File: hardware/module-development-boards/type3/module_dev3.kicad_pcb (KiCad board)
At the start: 2 copper layers, 30 x 26 mm, 28 parts, among them J1 SensorHub_Module_CONN_V1, J12 Conn_01x01, J13 Conn_01x01, J14 Conn_01x01, J15 Conn_01x01, J16 Conn_01x01, J17 Conn_01x01, J18 Conn_01x01, J19 Conn_01x01, J21 Conn_01x01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

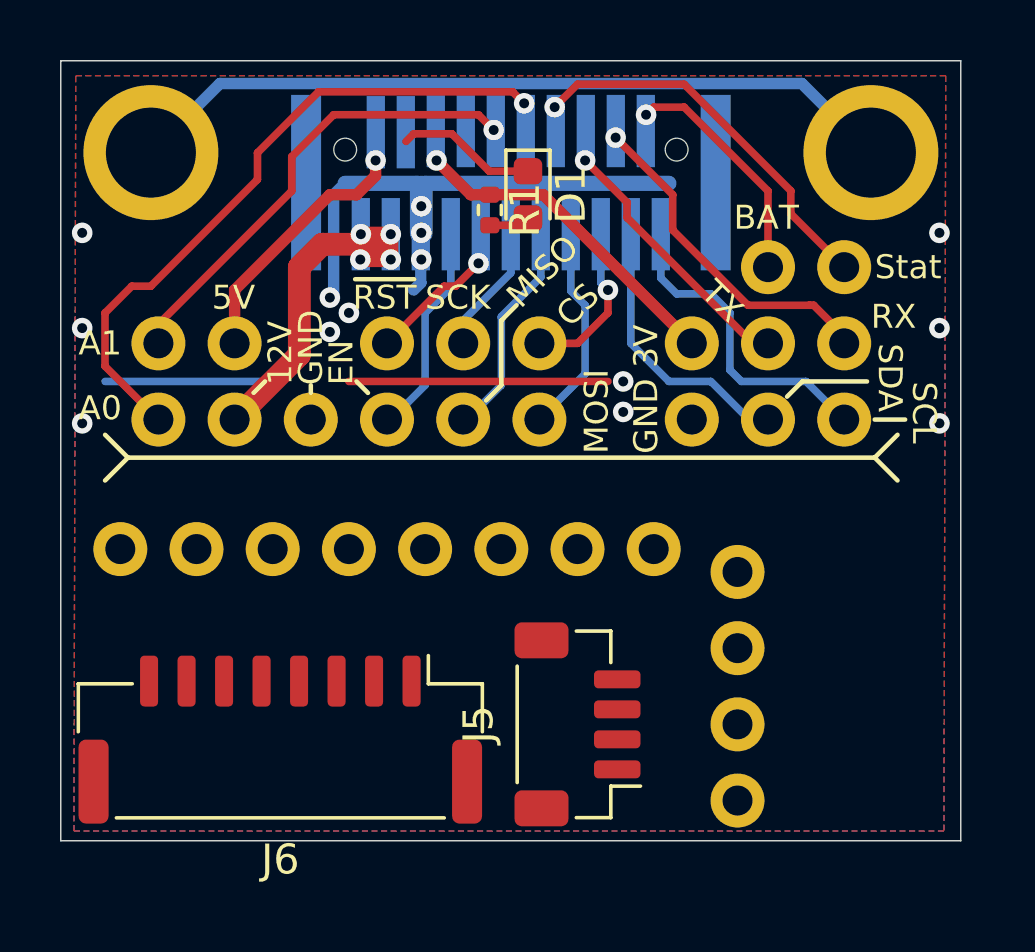
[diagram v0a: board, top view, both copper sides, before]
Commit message: cleanup dev board type 3
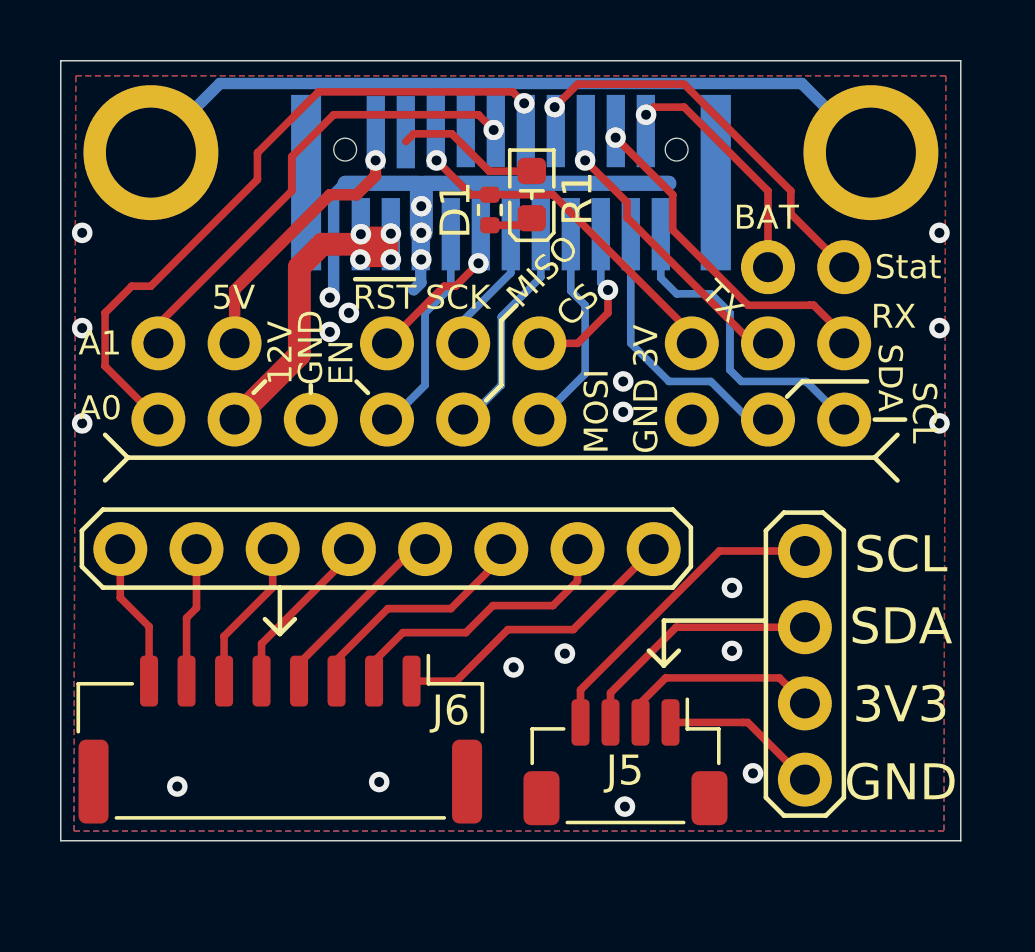
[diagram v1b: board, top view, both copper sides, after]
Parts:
- D1: value D_LED_0603_Red -> LED_0603_Red; footprint LED_SMD:LED_0603_1608Metric -> jlcsmt:LED_0603_1608Metric
- J1: value SensorHub_Module_CONN_V1 -> LegoSENSE_Module_CONN_V1
- moved J3 8.62 mm to (116.8, 77.3), turned to 0 degrees
- moved J5 2.04 mm to (110.8, 84.3), turned to 180 degrees
- moved D1 0.13 mm to (107.7, 65.4), turned to 90 degrees
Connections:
- net /~RST renamed /~{RST}
- D1 pad 2: Net-(D1-Pad2) -> (no net)
- R1 pad 2: Net-(D1-Pad2) -> (no net)
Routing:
- net GND: track 65.5 -> 49.0 mm, vias 14 -> 22
- net Net-(J3-Pad1): track 0.00 -> 10.5 mm
- net Net-(J4-Pad8): track 0.00 -> 9.89 mm
- net Net-(J4-Pad7): track 0.00 -> 9.61 mm
- net Net-(J3-Pad2): track 0.00 -> 8.37 mm
- net Net-(J4-Pad6): track 0.00 -> 7.90 mm
- net Net-(J3-Pad3): track 0.00 -> 6.83 mm
- net Net-(J4-Pad5): track 0.00 -> 6.37 mm
- net Net-(J4-Pad4): track 0.00 -> 5.61 mm
- net Net-(J3-Pad4): track 0.00 -> 5.27 mm
- net Net-(J4-Pad3): track 0.00 -> 5.07 mm
- net Net-(J4-Pad1): track 0.00 -> 4.80 mm
- net Net-(J4-Pad2): track 0.00 -> 4.54 mm
- net (no net): track 0.00 -> 1.49 mm
- net Net-(D1-Pad2): track 1.37 -> 0.00 mm
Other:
- net class Default removed
- board text added: "3V3"
- board text added: "~{RST}"
- board text removed: "~RST"
